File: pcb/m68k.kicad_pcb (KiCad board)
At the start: 2 copper layers, 116 parts, among them J1 USB_B_Micro, J3 SD_Card, J4 DB15_Male_HighDensity, J5 FTSH-105-01-L-DV-K, J6 FTSH-105-01-L-DV-K, J7 FTSH-105-01-L-DV-K, U1 93LC56, U10 25LCxxx, U11 TXB0108DQSR, U12 TXB0108DQSR, U13 iCE40-HX4K-TQ144, U14 ADV7125KSTZ50, U15 74LVC1G17, U16 LD1117S33TR_SOT223, U17 LD1117S12TR_SOT223, U18 ATL431BQDBZR, U2 68000D, U3 FT2232H, U4 TXB0108DQSR, U5 TXB0108DQSR, U6 TXB0108DQSR, U7 SN74LVC8T245PWR, U8 SN74LVC8T245PWR, U9 AS6C1616, X1 ASV-12.000MHz

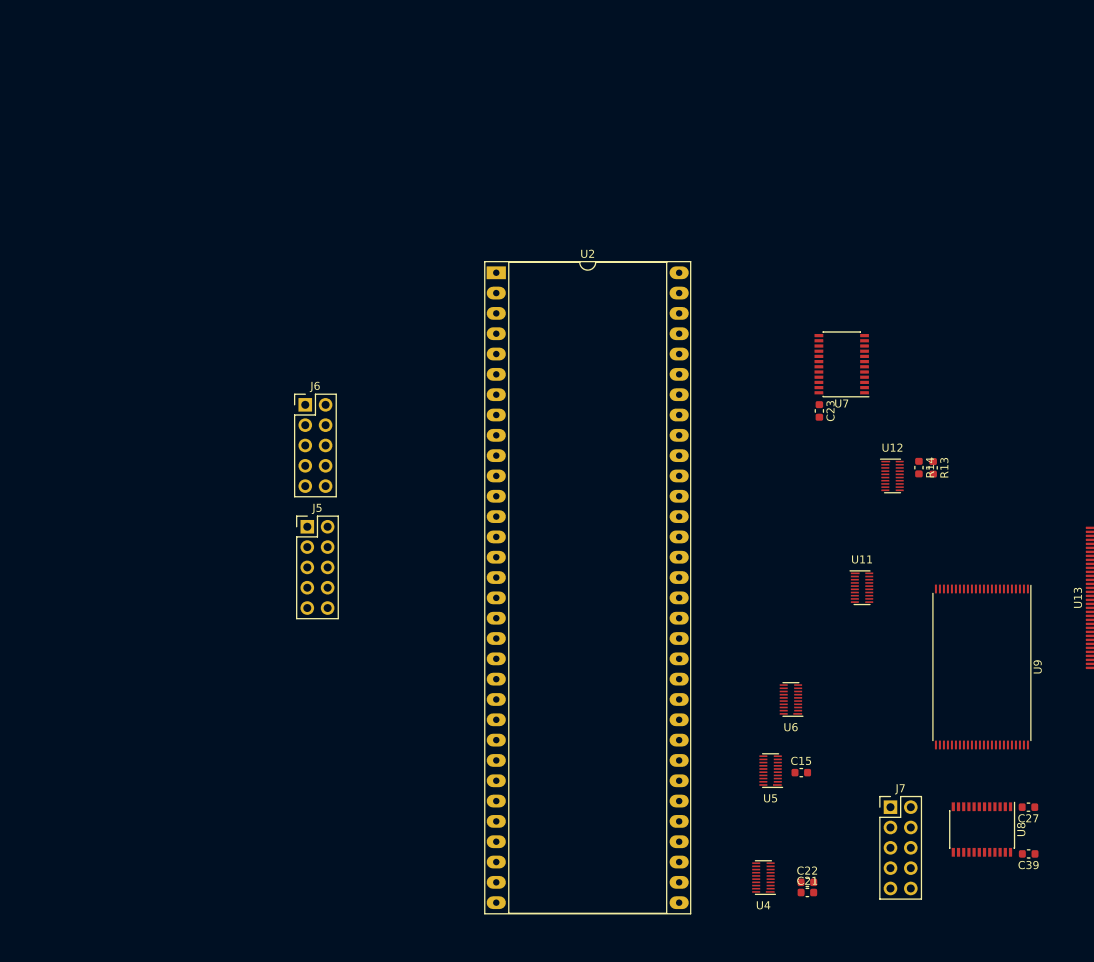
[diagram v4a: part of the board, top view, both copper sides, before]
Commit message: Added board outline
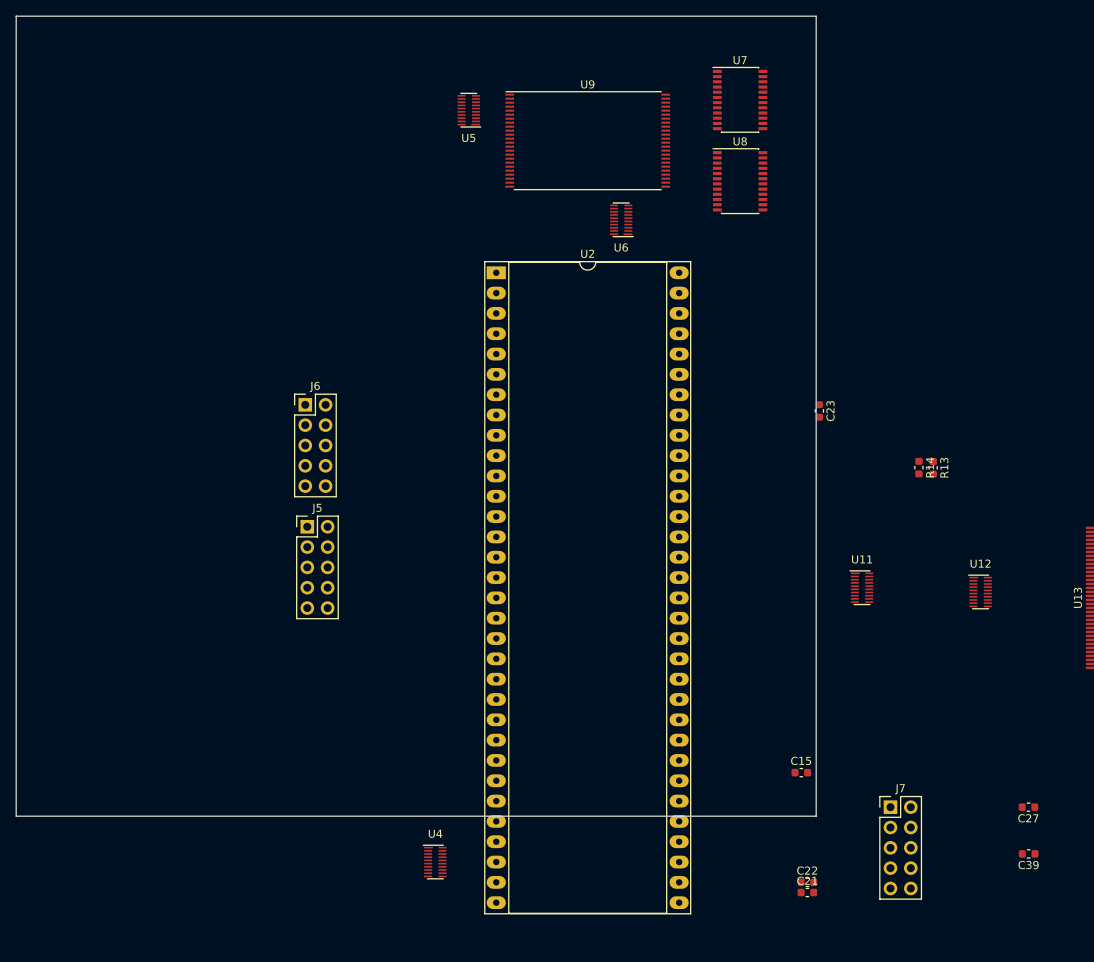
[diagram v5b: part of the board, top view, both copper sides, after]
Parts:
- moved U5 90.8 mm to (76.6, 31.8)
- moved U8 86.5 mm to (110.5, 40.6), turned to 0 degrees
- moved U9 82.2 mm to (91.4, 35.6), turned to 0 degrees
- moved U6 63.6 mm to (95.6, 45.5)
- moved U4 41.1 mm to (72.4, 125.7), turned to 0 degrees
- moved U7 35.4 mm to (110.5, 30.5), turned to 0 degrees
- moved U12 18.2 mm to (140.6, 92.0)
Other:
- board outline added: 100 x 100 mm

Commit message: arrange pcb
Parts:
- moved U13 101.7 mm to (78.5, 39.4)
- moved C6 93.1 mm to (177.0, 48.0)
- moved C8 93.1 mm to (177.0, 49.5)
- moved C2 93.1 mm to (150.4, 75.7)
- moved C4 93.1 mm to (158.5, 60.2)
- moved R15 93.1 mm to (166.9, 54.4)
- moved R8 93.1 mm to (171.4, 47.0)
- moved U3 93.1 mm to (168.1, 63.0)
- moved C1 93.1 mm to (150.4, 74.2)
- moved C10 93.1 mm to (152.9, 66.0)
- moved C3 93.1 mm to (157.2, 60.2)
- moved C5 93.1 mm to (177.0, 52.6)
- moved C7 93.1 mm to (177.0, 51.1)
- moved C9 93.1 mm to (152.9, 64.3)
- moved J1 93.1 mm to (189.7, 63.0)
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
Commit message: switch to micro sd
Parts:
- removed J3: SD_Card, Connector_Card:SD_TE_2041021
- added J8: Micro_SD_Card, Connector_Card:microSD_HC_Hirose_DM3AT-SF-PEJM5, F.Cu at (109.7, 62.5)
- moved C11 113.7 mm to (137.2, 60.5)
- moved C12 113.7 mm to (137.2, 68.1)
- moved C13 113.7 mm to (137.2, 58.9)
- moved C14 113.7 mm to (137.2, 66.5)
- moved C16 113.7 mm to (137.2, 69.6)
- moved C24 113.7 mm to (137.2, 55.9)
- moved C25 113.7 mm to (144.8, 81.5)
- moved C28 113.7 mm to (144.8, 68.8)
- moved C30 113.7 mm to (137.2, 57.4)
- moved C31 113.7 mm to (144.8, 78.2)
- moved C36 113.7 mm to (137.2, 63.5)
- moved C37 113.7 mm to (137.2, 62.0)
- moved C38 113.7 mm to (144.8, 75.2)
- moved C40 113.7 mm to (137.2, 52.8)
- moved C41 113.7 mm to (144.8, 73.7)
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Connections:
- J1 pad 4: (no net) -> Net-(J1-Pad4)
- J4 pad 11: (no net) -> Net-(J4-Pad11)
- J4 pad 12: (no net) -> Net-(J4-Pad12)
- J4 pad 15: (no net) -> Net-(J4-Pad15)
- J4 pad 4: (no net) -> Net-(J4-Pad4)
- J4 pad 6: (no net) -> Net-(J4-Pad6)
- J4 pad 7: (no net) -> Net-(J4-Pad7)
- J4 pad 8: (no net) -> Net-(J4-Pad8)
- J7 pad 7: (no net) -> Net-(J7-Pad7)
- J7 pad 9: (no net) -> Net-(J7-Pad9)
- U1 pad 7: (no net) -> Net-(U1-Pad7)
- U11 pad 10: (no net) -> Net-(U11-Pad10)
- U11 pad 12: (no net) -> Net-(U11-Pad12)
- U11 pad 13: (no net) -> Net-(U11-Pad13)
- U11 pad 9: (no net) -> Net-(U11-Pad9)
- U13 pad 109: (no net) -> Net-(U13-Pad109)
- U13 pad 133: (no net) -> Net-(U13-Pad133)
- U13 pad 25: (no net) -> Net-(U13-Pad25)
- U13 pad 35: (no net) -> Net-(U13-Pad35)
- U13 pad 36: (no net) -> Net-(U13-Pad36)
- U13 pad 50: (no net) -> Net-(U13-Pad50)
- U13 pad 51: (no net) -> Net-(U13-Pad51)
- U13 pad 58: (no net) -> Net-(U13-Pad58)
- U13 pad 77: (no net) -> Net-(U13-Pad77)
- U3 pad 19: (no net) -> Net-(U3-Pad19)
- U3 pad 22: (no net) -> Net-(U3-Pad22)
- U3 pad 26: (no net) -> Net-(U3-Pad26)
- U3 pad 27: (no net) -> Net-(U3-Pad27)
- U3 pad 28: (no net) -> Net-(U3-Pad28)
- U3 pad 29: (no net) -> Net-(U3-Pad29)
- U3 pad 3: (no net) -> Net-(U3-Pad3)
- U3 pad 30: (no net) -> Net-(U3-Pad30)
- U3 pad 32: (no net) -> Net-(U3-Pad32)
- U3 pad 33: (no net) -> Net-(U3-Pad33)
- U3 pad 34: (no net) -> Net-(U3-Pad34)
- U3 pad 36: (no net) -> Net-(U3-Pad36)
- U3 pad 40: (no net) -> Net-(U3-Pad40)
- U3 pad 41: (no net) -> Net-(U3-Pad41)
- U3 pad 43: (no net) -> Net-(U3-Pad43)
- U3 pad 44: (no net) -> Net-(U3-Pad44)
- U3 pad 45: (no net) -> Net-(U3-Pad45)
- U3 pad 46: (no net) -> Net-(U3-Pad46)
- U3 pad 48: (no net) -> Net-(U3-Pad48)
- U3 pad 52: (no net) -> Net-(U3-Pad52)
- U3 pad 53: (no net) -> Net-(U3-Pad53)
- U3 pad 54: (no net) -> Net-(U3-Pad54)
- U3 pad 55: (no net) -> Net-(U3-Pad55)
- U3 pad 57: (no net) -> Net-(U3-Pad57)
- U3 pad 58: (no net) -> Net-(U3-Pad58)
- U3 pad 59: (no net) -> Net-(U3-Pad59)
- U3 pad 60: (no net) -> Net-(U3-Pad60)
- U6 pad 10: (no net) -> Net-(U6-Pad10)
- U6 pad 12: (no net) -> Net-(U6-Pad12)
- U9 pad 10: (no net) -> Net-(U9-Pad10)
- U9 pad 13: (no net) -> Net-(U9-Pad13)
- U9 pad 47: (no net) -> Net-(U9-Pad47)

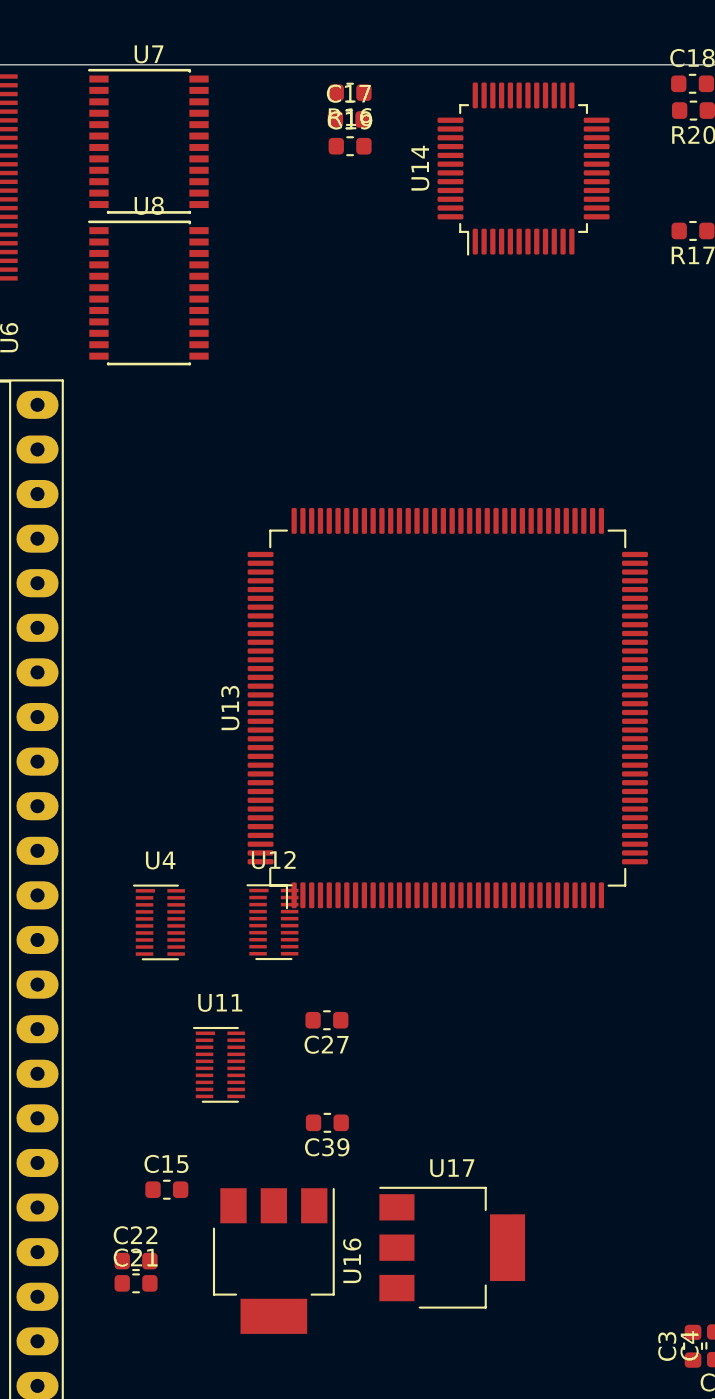
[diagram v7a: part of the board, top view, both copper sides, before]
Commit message: fix vga pinout
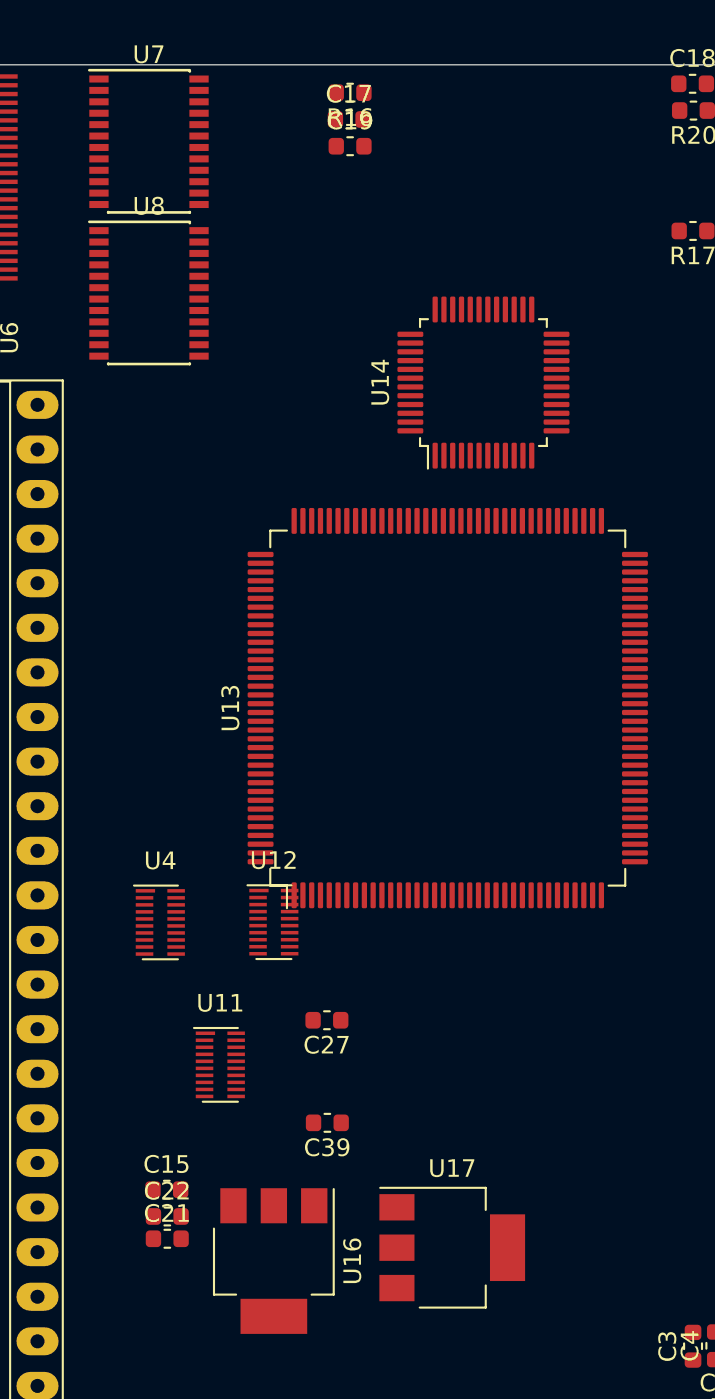
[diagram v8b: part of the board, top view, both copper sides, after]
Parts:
- moved U14 12.4 mm to (78.7, 38.1)
- moved C21 3.10 mm to (60.7, 86.9)
- moved C22 3.10 mm to (60.7, 85.6)
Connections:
- U13 pad 101: /b7 -> /r0
- U13 pad 73: /r0 -> /b7
- U13 pad 74: /r1 -> /b6
- U13 pad 75: /r2 -> /b5
- U13 pad 76: /r3 -> /b4
- U13 pad 78: /r4 -> /b3
- U13 pad 79: /r5 -> /b2
- U13 pad 80: /r6 -> /b1
- U13 pad 81: /r7 -> /b0
- U13 pad 82: /g0 -> /g7
- U13 pad 83: /g1 -> /g6
- U13 pad 84: /g2 -> /g5
- U13 pad 85: /g3 -> /g4
- U13 pad 87: /g4 -> /g3
- U13 pad 88: /g5 -> /g2
- U13 pad 90: /g6 -> /g1
- U13 pad 91: /g7 -> /g0
- U13 pad 93: /b0 -> /r7
- U13 pad 94: /b1 -> /r6
- U13 pad 95: /b2 -> /r5
- U13 pad 96: /b3 -> /r4
- U13 pad 97: /b4 -> /r3
- U13 pad 98: /b5 -> /r2
- U13 pad 99: /b6 -> /r1
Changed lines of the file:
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@@
   )
   (module Capacitor_SMD:C_0603_1608Metric (layer F.Cu)
-    (at 58.9535 89.408)
+    (at 60.7315 86.868)
     (descr "Capacitor SMD 0603 (1608 Metric), square (rectangular) end terminal, IPC_7351 nominal, (Body size source: http://www.tortai-tech.com/upload/download/2011102023233369053.pdf), generated with kicad-footprint-generator")
     (tags capacitor)
@@
   )
   (module Capacitor_SMD:C_0603_1608Metric (layer F.Cu)
-    (at 58.9535 88.138)
+    (at 60.7315 85.598)
     (descr "Capacitor SMD 0603 (1608 Metric), square (rectangular) end terminal, IPC_7351 nominal, (Body size source: http://www.tortai-tech.com/upload/download/2011102023233369053.pdf), generated with kicad-footprint-generator")
     (tags capacitor)
@@
       (net 2 +3V3))
     (pad 73 smd roundrect (at 10.6625 8.75 90) (size 1.475 0.3) (layers F.Cu F.Paste F.Mask) (roundrect_rratio 0.25)
-      (net 178 /r0))
+      (net 155 /b7))
     (pad 74 smd roundrect (at 10.6625 8.25 90) (size 1.475 0.3) (layers F.Cu F.Paste F.Mask) (roundrect_rratio 0.25)
-      (net 177 /r1))
+      (net 156 /b6))
     (pad 75 smd roundrect (at 10.6625 7.75 90) (size 1.475 0.3) (layers F.Cu F.Paste F.Mask) (roundrect_rratio 0.25)
-      (net 176 /r2))
+      (net 157 /b5))
     (pad 76 smd roundrect (at 10.6625 7.25 90) (size 1.475 0.3) (layers F.Cu F.Paste F.Mask) (roundrect_rratio 0.25)
-      (net 175 /r3))
+      (net 158 /b4))
     (pad 77 smd roundrect (at 10.6625 6.75 90) (size 1.475 0.3) (layers F.Cu F.Paste F.Mask) (roundrect_rratio 0.25)
       (net 242 "Net-(U13-Pad77)"))
     (pad 78 smd roundrect (at 10.6625 6.25 90) (size 1.475 0.3) (layers F.Cu F.Paste F.Mask) (roundrect_rratio 0.25)
-      (net 174 /r4))
+      (net 159 /b3))
     (pad 79 smd roundrect (at 10.6625 5.75 90) (size 1.475 0.3) (layers F.Cu F.Paste F.Mask) (roundrect_rratio 0.25)
-      (net 173 /r5))
+      (net 160 /b2))
     (pad 80 smd roundrect (at 10.6625 5.25 90) (size 1.475 0.3) (layers F.Cu F.Paste F.Mask) (roundrect_rratio 0.25)
-      (net 172 /r6))
+      (net 161 /b1))
     (pad 81 smd roundrect (at 10.6625 4.75 90) (size 1.475 0.3) (layers F.Cu F.Paste F.Mask) (roundrect_rratio 0.25)
-      (net 171 /r7))
+      (net 162 /b0))
     (pad 82 smd roundrect (at 10.6625 4.25 90) (size 1.475 0.3) (layers F.Cu F.Paste F.Mask) (roundrect_rratio 0.25)
-      (net 170 /g0))
+      (net 163 /g7))
     (pad 83 smd roundrect (at 10.6625 3.75 90) (size 1.475 0.3) (layers F.Cu F.Paste F.Mask) (roundrect_rratio 0.25)
-      (net 169 /g1))
+      (net 164 /g6))
     (pad 84 smd roundrect (at 10.6625 3.25 90) (size 1.475 0.3) (layers F.Cu F.Paste F.Mask) (roundrect_rratio 0.25)
-      (net 168 /g2))
+      (net 165 /g5))
     (pad 85 smd roundrect (at 10.6625 2.75 90) (size 1.475 0.3) (layers F.Cu F.Paste F.Mask) (roundrect_rratio 0.25)
-      (net 167 /g3))
+      (net 166 /g4))
     (pad 86 smd roundrect (at 10.6625 2.25 90) (size 1.475 0.3) (layers F.Cu F.Paste F.Mask) (roundrect_rratio 0.25)
       (net 1 GND))
     (pad 87 smd roundrect (at 10.6625 1.75 90) (size 1.475 0.3) (layers F.Cu F.Paste F.Mask) (roundrect_rratio 0.25)
-      (net 166 /g4))
+      (net 167 /g3))
     (pad 88 smd roundrect (at 10.6625 1.25 90) (size 1.475 0.3) (layers F.Cu F.Paste F.Mask) (roundrect_rratio 0.25)
-      (net 165 /g5))
+      (net 168 /g2))
     (pad 89 smd roundrect (at 10.6625 0.75 90) (size 1.475 0.3) (layers F.Cu F.Paste F.Mask) (roundrect_rratio 0.25)
       (net 2 +3V3))
     (pad 90 smd roundrect (at 10.6625 0.25 90) (size 1.475 0.3) (layers F.Cu F.Paste F.Mask) (roundrect_rratio 0.25)
-      (net 164 /g6))
+      (net 169 /g1))
     (pad 91 smd roundrect (at 10.6625 -0.25 90) (size 1.475 0.3) (layers F.Cu F.Paste F.Mask) (roundrect_rratio 0.25)
-      (net 163 /g7))
+      (net 170 /g0))
     (pad 92 smd roundrect (at 10.6625 -0.75 90) (size 1.475 0.3) (layers F.Cu F.Paste F.Mask) (roundrect_rratio 0.25)
       (net 9 +1V2))
     (pad 93 smd roundrect (at 10.6625 -1.25 90) (size 1.475 0.3) (layers F.Cu F.Paste F.Mask) (roundrect_rratio 0.25)
-      (net 162 /b0))
+      (net 171 /r7))
     (pad 94 smd roundrect (at 10.6625 -1.75 90) (size 1.475 0.3) (layers F.Cu F.Paste F.Mask) (roundrect_rratio 0.25)
-      (net 161 /b1))
+      (net 172 /r6))
     (pad 95 smd roundrect (at 10.6625 -2.25 90) (size 1.475 0.3) (layers F.Cu F.Paste F.Mask) (roundrect_rratio 0.25)
-      (net 160 /b2))
+      (net 173 /r5))
     (pad 96 smd roundrect (at 10.6625 -2.75 90) (size 1.475 0.3) (layers F.Cu F.Paste F.Mask) (roundrect_rratio 0.25)
-      (net 159 /b3))
+      (net 174 /r4))
     (pad 97 smd roundrect (at 10.6625 -3.25 90) (size 1.475 0.3) (layers F.Cu F.Paste F.Mask) (roundrect_rratio 0.25)
-      (net 158 /b4))
+      (net 175 /r3))
     (pad 98 smd roundrect (at 10.6625 -3.75 90) (size 1.475 0.3) (layers F.Cu F.Paste F.Mask) (roundrect_rratio 0.25)
-      (net 157 /b5))
+      (net 176 /r2))
     (pad 99 smd roundrect (at 10.6625 -4.25 90) (size 1.475 0.3) (layers F.Cu F.Paste F.Mask) (roundrect_rratio 0.25)
-      (net 156 /b6))
+      (net 177 /r1))
     (pad 100 smd roundrect (at 10.6625 -4.75 90) (size 1.475 0.3) (layers F.Cu F.Paste F.Mask) (roundrect_rratio 0.25)
       (net 2 +3V3))
     (pad 101 smd roundrect (at 10.6625 -5.25 90) (size 1.475 0.3) (layers F.Cu F.Paste F.Mask) (roundrect_rratio 0.25)
-      (net 155 /b7))
+      (net 178 /r0))
     (pad 102 smd roundrect (at 10.6625 -5.75 90) (size 1.475 0.3) (layers F.Cu F.Paste F.Mask) (roundrect_rratio 0.25)
       (net 154 "Net-(U13-Pad102)"))
@@
   )
   (module Package_QFP:LQFP-48_7x7mm_P0.5mm (layer F.Cu)
-    (at 81.026 25.908 90)
+    (at 78.74 38.1 90)
     (descr "LQFP, 48 Pin (https://www.analog.com/media/en/technical-documentation/data-sheets/ltc2358-16.pdf), generated with kicad-footprint-generator ipc_gullwing_generator.py")
     (tags "LQFP QFP")
@@
     (fp_line (start 3.75 3.15) (end 5.15 3.15) (layer F.CrtYd) (width 0.05))
     (fp_line (start 5.15 3.15) (end 5.15 0) (layer F.CrtYd) (width 0.05))
-    (fp_text user %R (at 0 0 90) (layer F.Fab)
+    (fp_text user %R (at 0 -0.254 90) (layer F.Fab)
       (effects (font (size 1 1) (thickness 0.15)))
     )
